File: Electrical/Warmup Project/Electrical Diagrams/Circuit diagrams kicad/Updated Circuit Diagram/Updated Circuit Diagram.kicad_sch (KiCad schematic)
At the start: 26 parts, among them M1 Motor_DC, M2 Motor_DC, M3 Motor_DC, U3 MCP2562-H_SN, U4 Teensy4.1, U5 MCP2562-H_SN, U7 MCP2562-H_SN, U8 HX711, U9 HX711

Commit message: Hopefully working?
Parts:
- removed R2, R3, R4, R5: R_45deg, symbol Device:R_45deg
- removed U8, U9: HX711, SEN-13879:SPARKFUN_SEN-13879, symbol SEN-13879:SEN-13879
- added R10, R11, R12, R9: R_45deg, symbol Device:R_45deg
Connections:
- new net: AMT213D-V2. (GND), U6. (x2)
- new net: R10.2, R12.1
- new net: R11.2, R12.2
- new net: R10.1, R9.1
- new net: R11.1, R9.2
- new net: AMT213D-V1. (GND), U2. (x2)
- new net: AMT213D-V. (GND), U1. (x2)
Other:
- moved on the sheet: AMT213D-V, AMT213D-V1, AMT213D-V2, E_STOP, E_STOP1, E_STOP2, U4

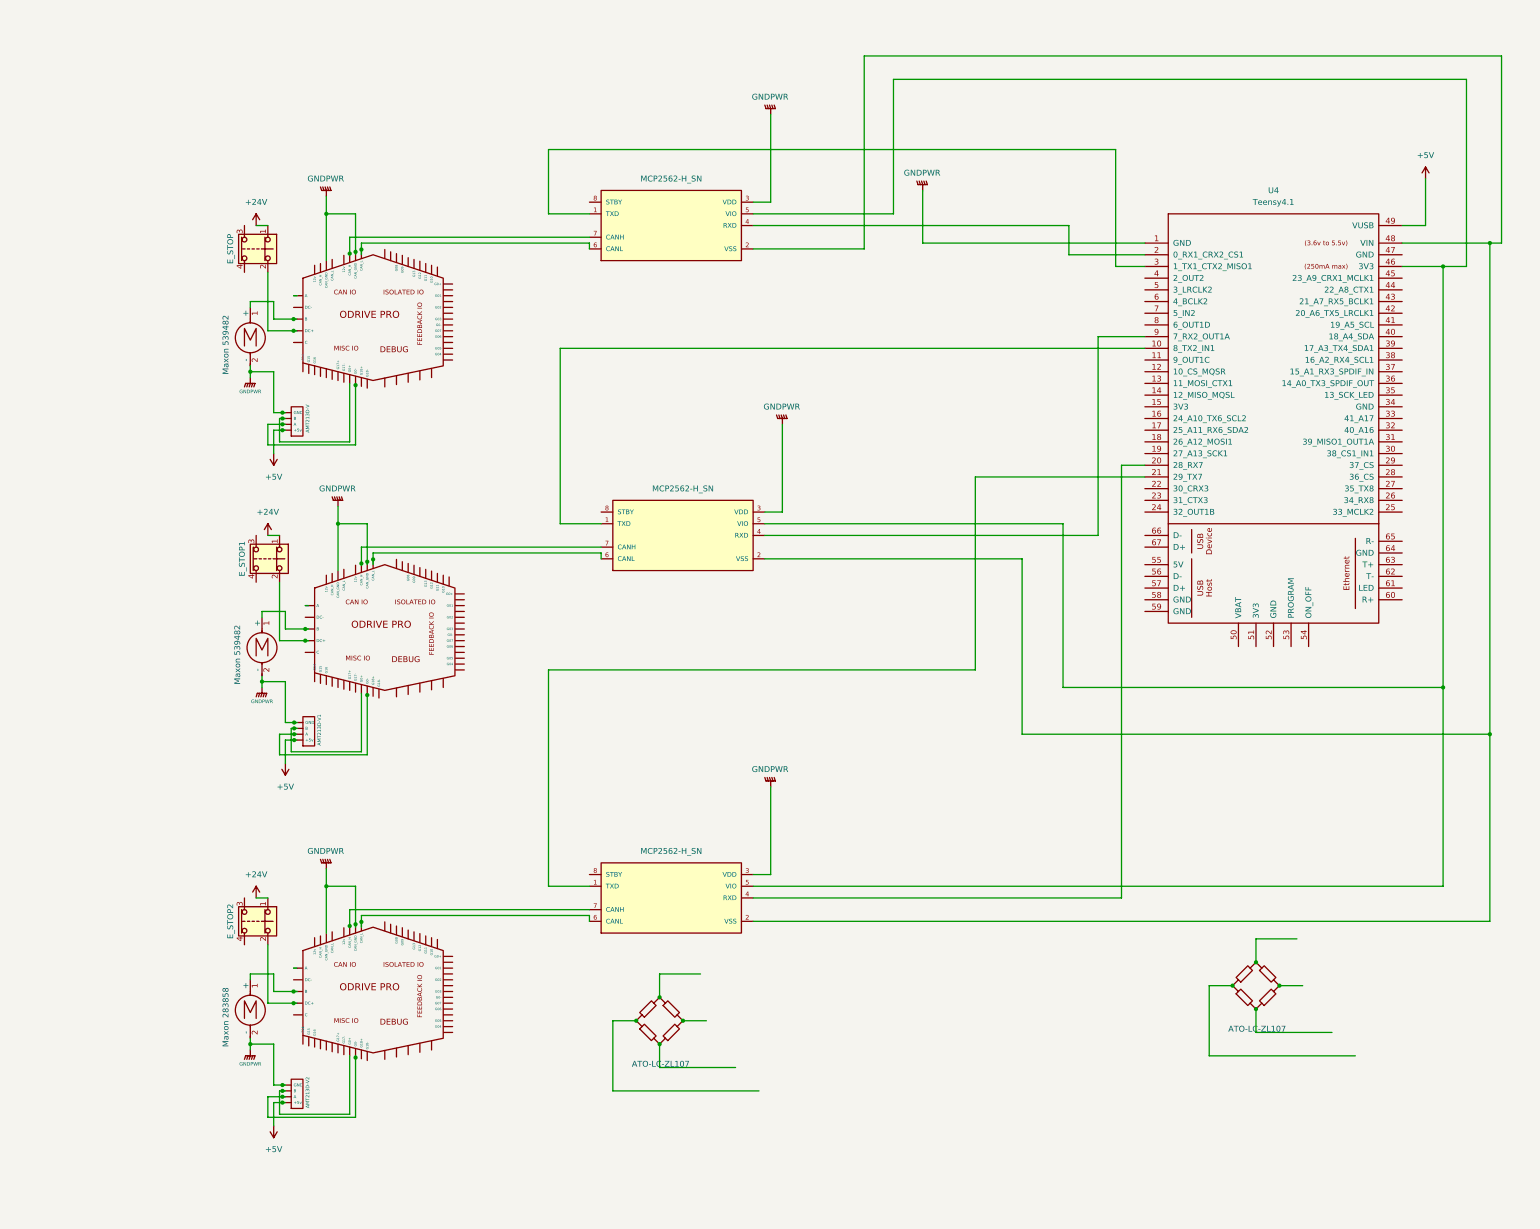
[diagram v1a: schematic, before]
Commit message: Schematic Updates
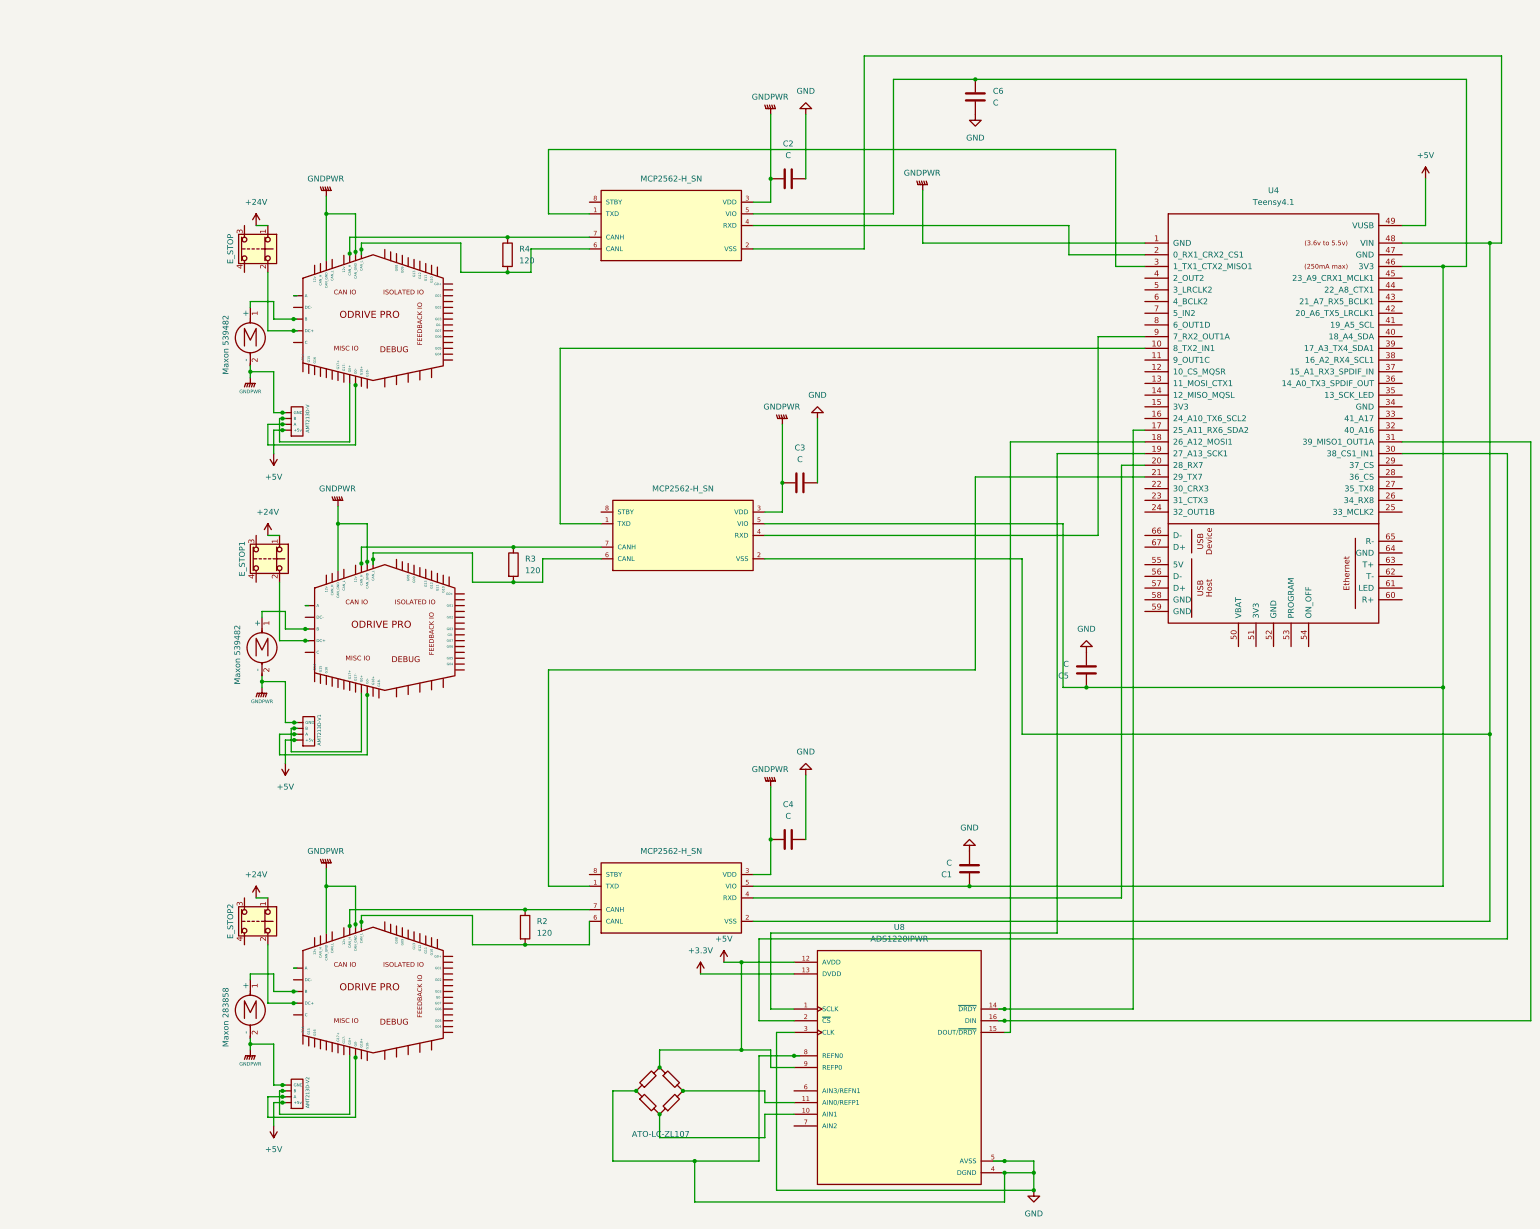
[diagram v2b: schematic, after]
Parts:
- removed R10, R11, R12, R9: R_45deg, symbol Device:R_45deg
- added C1, C2, C3, C4, C5, C6: C, symbol Device:C
- added R2, R3, R4: 120, symbol Device:R
- added U8: ADS1220IPWR, ADS1220IPWR:SOP65P640X120-16N, symbol ADS1220IPWR:ADS1220IPWR
- AMT213D-V, AMT213D-V1, AMT213D-V2, U1, U2, U6: value ~ -> (none)
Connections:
- net +5V: now also R1.2, R7.1, U8.12 (AVDD), U8.9 (REFP0)
- net GNDPWR: now also C2.1, C3.1, C4.1
- net at U6., U7.6 (CANL): now also R2.2
- net at U6., U7.7 (CANH): now also R2.1
- net GND: now reaches R1.1, R6.1
- net GND: now also C1.2, C2.2, C3.2, C4.2, C5.2, C6.2, U8.3 (CLK), U8.4 (DGND), U8.5 (AVSS), U8.8 (REFN0)
- net at R6.2, R8.1: now also U8.10 (AIN1)
- net at R7.2, R8.2: now also U8.11 (AIN0/REFP1)
- net at U3.5 (VIO), U4.46 (3V3), U5.5 (VIO)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: now also C1.1, C5.1, C6.1
- net at U1., U5.6 (CANL): now also R4.2
- net at U1., U5.7 (CANH): now also R4.1
- net at U4.17 (25_A11_RX6_SDA2): now also U8.14 (~{DRDY})
- net at U4.18 (26_A12_MOSI1): now also U8.15 (DOUT/~{DRDY})
- net at U4.19 (27_A13_SCK1): now also U8.1 (SCLK)
- net at U4.30 (38_CS1_IN1): now also U8.2 (~{CS})
- net at U4.31 (39_MISO1_OUT1A): now also U8.16 (DIN)
- net at U2., U3.6 (CANL): now also R3.2
- net at U2., U3.7 (CANH): now also R3.1
- new net: AMT213D-V2. (GND), U6. (x2)
- new net: AMT213D-V1. (GND), U2. (x2)
- new net: AMT213D-V. (GND), U1. (x2)
- new net +3.3V: U8.13 (DVDD)
